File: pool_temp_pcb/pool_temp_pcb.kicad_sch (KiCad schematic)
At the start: 9 parts, among them U1 MAX7221xNG, U2 PicoW

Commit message: Update schematic
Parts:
- R1, R2, R3, R4: renamed from R?; footprint (none) -> Resistor_THT:R_Axial_DIN0411_L9.9mm_D3.6mm_P15.24mm_Horizontal
- U3, U4: renamed from U?; footprint (none) -> seven_segment:ATA8041AB
- gave numbers to parts that had none: 1

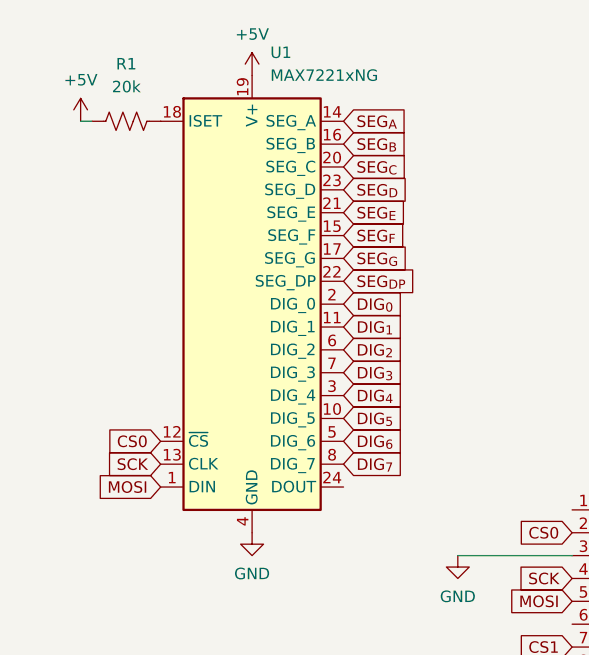
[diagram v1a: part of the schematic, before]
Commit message: Add trim pot
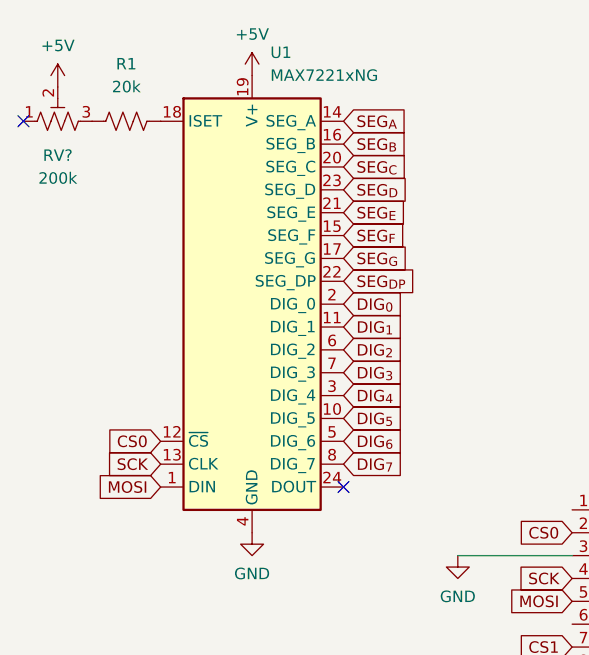
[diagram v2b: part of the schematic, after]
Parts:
- added RV?: 200k, symbol Device:R_Potentiometer_Trim_US
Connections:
- net +5V: now also RV?.2; no longer R1.1
- new net: R1.1, RV?.3
- no-connect marks 0 -> 2
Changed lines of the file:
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@@
   (junction (at 143.51 86.36) (diameter 0) (color 0 0 0 0)
   )
+  (no_connect (at 22.86 38.1))
+  (no_connect (at 58.42 78.74))
   (wire (pts (xy 125.476 81.28) (xy 119.38 81.28))
     (stroke (width 0) (type default) (color 0 0 0 0))
@@
   )
   (wire (pts (xy 143.51 96.52) (xy 147.32 96.52))
-    (stroke (width 0) (type default) (color 0 0 0 0))
-  )
-  (wire (pts (xy 29.21 38.1) (xy 30.48 38.1))
     (stroke (width 0) (type default) (color 0 0 0 0))
   )
@@
     )
     (pin "1")
+  )
+  (symbol (lib_id "Device:R_Potentiometer_Trim_US") (at 26.67 38.1 90) (unit 1)
+    (in_bom yes) (on_board yes) (fields_autoplaced)
+    (property "Reference" "RV?" (id 0) (at 26.67 41.91 90))
+    (property "Value" "200k" (id 1) (at 26.67 44.45 90))
+    (property "Footprint" "" (id 2) (at 26.67 38.1 0)
+      (effects (font (size 1.27 1.27)) hide)
+    )
+    (property "Datasheet" "~" (id 3) (at 26.67 38.1 0)
+      (effects (font (size 1.27 1.27)) hide)
+    )
+    (pin "1")
+    (pin "2")
+    (pin "3")
   )
   (symbol (lib_id "RPi_Pico:PicoW") (at 101.6 105.41 0) (unit 1)
@@
     (pin "2")
   )
-  (symbol (lib_id "power:+5V") (at 29.21 38.1 0) (unit 1)
-    (in_bom yes) (on_board yes) (fields_autoplaced)
-    (property "Reference" "#PWR01" (id 0) (at 29.21 41.91 0)
-      (effects (font (size 1.27 1.27)) hide)
-    )
-    (property "Value" "+5V" (id 1) (at 29.21 33.528 0))
-    (property "Footprint" "" (id 2) (at 29.21 38.1 0)
-      (effects (font (size 1.27 1.27)) hide)
-    )
-    (property "Datasheet" "" (id 3) (at 29.21 38.1 0)
+  (symbol (lib_id "power:+5V") (at 26.67 34.29 0) (unit 1)
+    (in_bom yes) (on_board yes) (fields_autoplaced)
+    (property "Reference" "#PWR01" (id 0) (at 26.67 38.1 0)
+      (effects (font (size 1.27 1.27)) hide)
+    )
+    (property "Value" "+5V" (id 1) (at 26.67 29.718 0))
+    (property "Footprint" "" (id 2) (at 26.67 34.29 0)
+      (effects (font (size 1.27 1.27)) hide)
+    )
+    (property "Datasheet" "" (id 3) (at 26.67 34.29 0)
       (effects (font (size 1.27 1.27)) hide)
     )
@@
       (reference "R4") (unit 1) (value "10k") (footprint "Resistor_THT:R_Axial_DIN0411_L9.9mm_D3.6mm_P15.24mm_Horizontal")
     )
+    (path "/4106378e-7235-4e9b-81fd-86d6d668a59a"
+      (reference "RV?") (unit 1) (value "200k") (footprint "")
+    )
     (path "/a163b600-67df-462c-baf5-e9cae83b8f90"

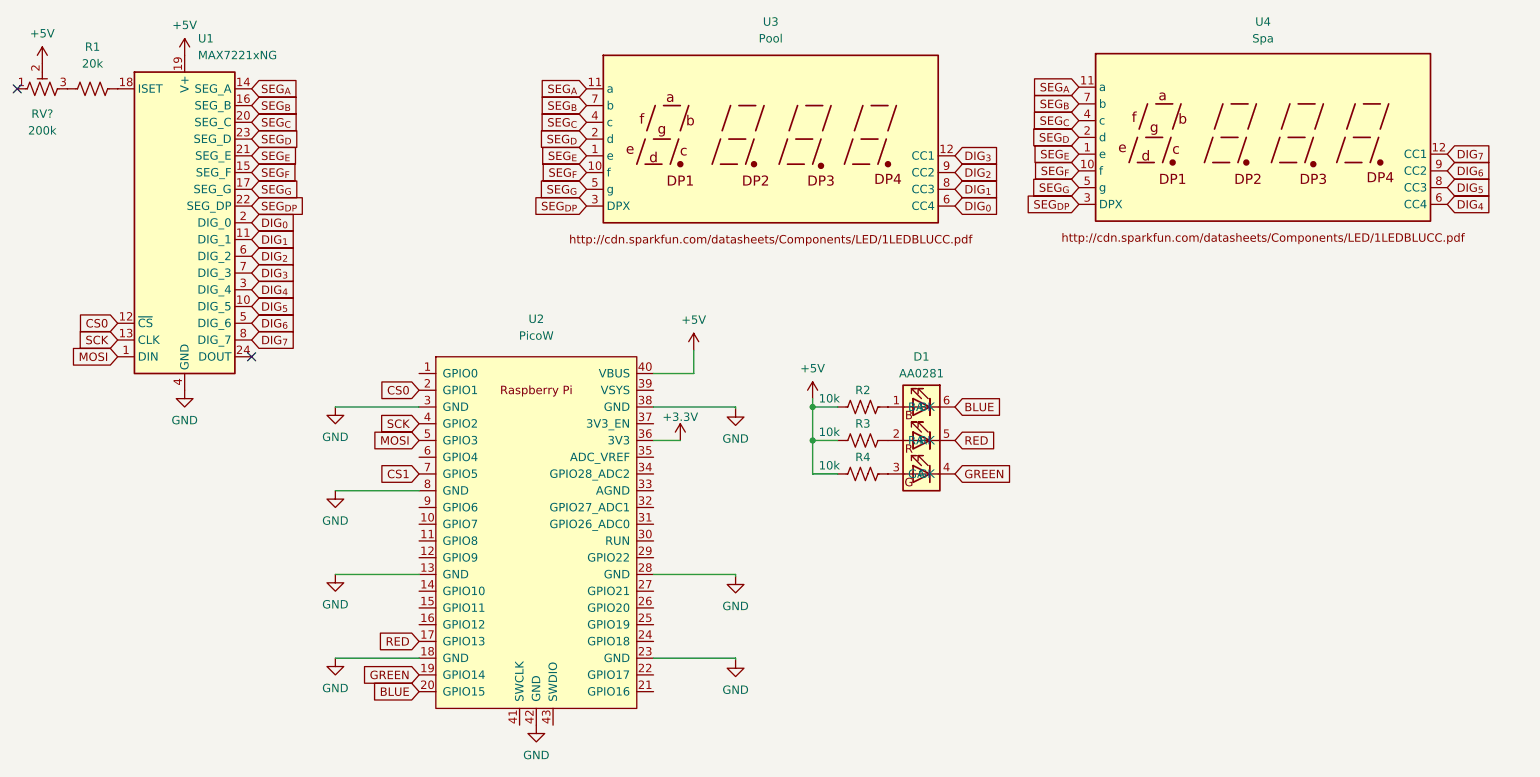
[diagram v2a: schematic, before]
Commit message: Layout version 1 of temperature pcb
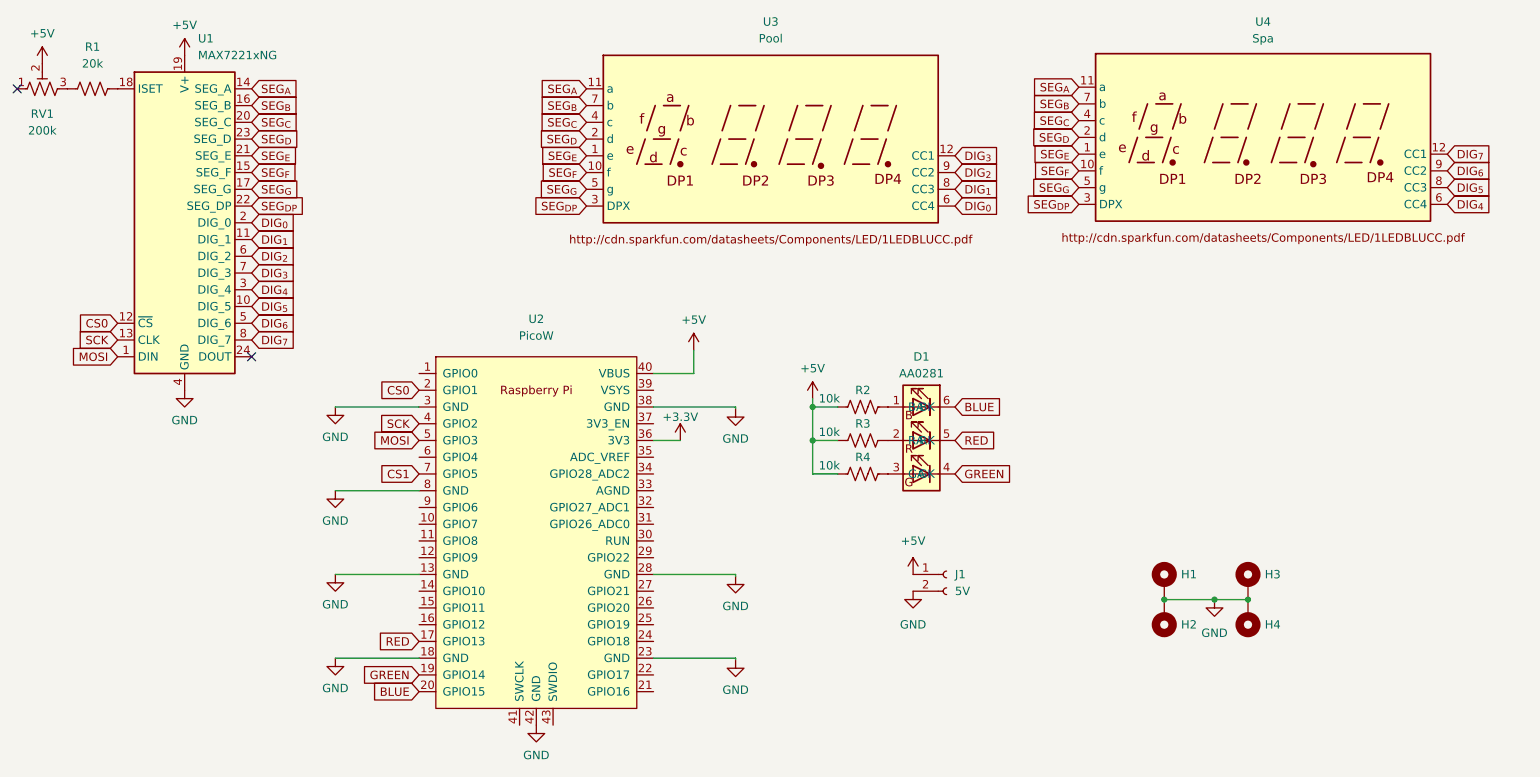
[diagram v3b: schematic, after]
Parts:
- added H1: Hole, MountingHole:MountingHole_3.2mm_M3_Pad_TopBottom, symbol Mechanical:MountingHole_Pad
- added H2, H3, H4: MountingHole_Pad, MountingHole:MountingHole_3.2mm_M3_Pad_TopBottom, symbol Mechanical:MountingHole_Pad
- added J1: 5V, Connector_PinHeader_2.54mm:PinHeader_1x02_P2.54mm_Vertical, symbol Connector:Conn_01x02_Female
- RV1: renamed from RV?; footprint (none) -> Potentiometer_THT:Potentiometer_Runtron_RM-065_Vertical
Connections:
- net +5V: now also J1.1 (Pin_1)
- net GND: now also H1.1, H2.1, H3.1, H4.1, J1.2 (Pin_2)
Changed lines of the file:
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@@
 (kicad_sch (version 20211123) (generator eeschema)
   (paper "A4")
+  (junction (at 204.47 115.57) (diameter 0) (color 0 0 0 0)
+  )
+  (junction (at 209.55 115.57) (diameter 0) (color 0 0 0 0)
+  )
   (junction (at 143.51 91.44) (diameter 0) (color 0 0 0 0)
   )
   (junction (at 143.51 86.36) (diameter 0) (color 0 0 0 0)
+  )
+  (junction (at 196.85 115.57) (diameter 0) (color 0 0 0 0)
   )
   (no_connect (at 22.86 38.1))
@@
     (stroke (width 0) (type default) (color 0 0 0 0))
   )
+  (wire (pts (xy 196.85 115.57) (xy 204.47 115.57))
+    (stroke (width 0) (type default) (color 0 0 0 0))
+  )
   (wire (pts (xy 131.826 111.76) (xy 131.826 112.014))
+    (stroke (width 0) (type default) (color 0 0 0 0))
+  )
+  (wire (pts (xy 204.47 115.57) (xy 209.55 115.57))
     (stroke (width 0) (type default) (color 0 0 0 0))
   )
@@
     )
     (property "Datasheet" "" (id 3) (at 131.826 112.014 0)
+      (effects (font (size 1.27 1.27)) hide)
+    )
+    (pin "1")
+  )
+  (symbol (lib_id "Mechanical:MountingHole_Pad") (at 196.85 113.03 0) (unit 1)
+    (in_bom yes) (on_board yes) (fields_autoplaced)
+    (property "Reference" "H1" (id 0) (at 199.39 111.7599 0)
+      (effects (font (size 1.27 1.27)) (justify left))
+    )
+    (property "Value" "Hole" (id 1) (at 199.39 113.0299 0)
+      (effects (font (size 1.27 1.27)) (justify left) hide)
+    )
+    (property "Footprint" "MountingHole:MountingHole_3.2mm_M3_Pad_TopBottom" (id 2) (at 196.85 113.03 0)
+      (effects (font (size 1.27 1.27)) hide)
+    )
+    (property "Datasheet" "~" (id 3) (at 196.85 113.03 0)
+      (effects (font (size 1.27 1.27)) hide)
+    )
+    (pin "1")
+  )
+  (symbol (lib_id "Mechanical:MountingHole_Pad") (at 209.55 118.11 180) (unit 1)
+    (in_bom yes) (on_board yes) (fields_autoplaced)
+    (property "Reference" "H4" (id 0) (at 212.09 119.3799 0)
+      (effects (font (size 1.27 1.27)) (justify right))
+    )
+    (property "Value" "MountingHole_Pad" (id 1) (at 212.09 120.6499 0)
+      (effects (font (size 1.27 1.27)) (justify right) hide)
+    )
+    (property "Footprint" "MountingHole:MountingHole_3.2mm_M3_Pad_TopBottom" (id 2) (at 209.55 118.11 0)
+      (effects (font (size 1.27 1.27)) hide)
+    )
+    (property "Datasheet" "~" (id 3) (at 209.55 118.11 0)
       (effects (font (size 1.27 1.27)) hide)
     )
@@
     (pin "1")
   )
+  (symbol (lib_id "power:GND") (at 158.75 114.3 0) (unit 1)
+    (in_bom yes) (on_board yes) (fields_autoplaced)
+    (property "Reference" "#PWR016" (id 0) (at 158.75 120.65 0)
+      (effects (font (size 1.27 1.27)) hide)
+    )
+    (property "Value" "GND" (id 1) (at 158.75 119.38 0))
+    (property "Footprint" "" (id 2) (at 158.75 114.3 0)
+      (effects (font (size 1.27 1.27)) hide)
+    )
+    (property "Datasheet" "" (id 3) (at 158.75 114.3 0)
+      (effects (font (size 1.27 1.27)) hide)
+    )
+    (pin "1")
+  )
   (symbol (lib_id "Device:R_Potentiometer_Trim_US") (at 26.67 38.1 90) (unit 1)
     (in_bom yes) (on_board yes) (fields_autoplaced)
-    (property "Reference" "RV?" (id 0) (at 26.67 41.91 90))
+    (property "Reference" "RV1" (id 0) (at 26.67 41.91 90))
     (property "Value" "200k" (id 1) (at 26.67 44.45 90))
-    (property "Footprint" "" (id 2) (at 26.67 38.1 0)
+    (property "Footprint" "Potentiometer_THT:Potentiometer_Runtron_RM-065_Vertical" (id 2) (at 26.67 38.1 0)
       (effects (font (size 1.27 1.27)) hide)
     )
@@
     (pin "1")
   )
+  (symbol (lib_id "Connector:Conn_01x02_Female") (at 163.83 111.76 0) (unit 1)
+    (in_bom yes) (on_board yes) (fields_autoplaced)
+    (property "Reference" "J1" (id 0) (at 165.1 111.7599 0)
+      (effects (font (size 1.27 1.27)) (justify left))
+    )
+    (property "Value" "5V" (id 1) (at 165.1 114.2999 0)
+      (effects (font (size 1.27 1.27)) (justify left))
+    )
+    (property "Footprint" "Connector_PinHeader_2.54mm:PinHeader_1x02_P2.54mm_Vertical" (id 2) (at 163.83 111.76 0)
+      (effects (font (size 1.27 1.27)) hide)
+    )
+    (property "Datasheet" "~" (id 3) (at 163.83 111.76 0)
+      (effects (font (size 1.27 1.27)) hide)
+    )
+    (pin "1")
+    (pin "2")
+  )
   (symbol (lib_id "power:GND") (at 101.6 134.62 0) (unit 1)
     (in_bom yes) (on_board yes) (fields_autoplaced)
@@
     (pin "1")
   )
+  (symbol (lib_id "Mechanical:MountingHole_Pad") (at 196.85 118.11 180) (unit 1)
+    (in_bom yes) (on_board yes) (fields_autoplaced)
+    (property "Reference" "H2" (id 0) (at 199.39 119.3799 0)
+      (effects (font (size 1.27 1.27)) (justify right))
+    )
+    (property "Value" "MountingHole_Pad" (id 1) (at 199.39 120.6499 0)
+      (effects (font (size 1.27 1.27)) (justify right) hide)
+    )
+    (property "Footprint" "MountingHole:MountingHole_3.2mm_M3_Pad_TopBottom" (id 2) (at 196.85 118.11 0)
+      (effects (font (size 1.27 1.27)) hide)
+    )
+    (property "Datasheet" "~" (id 3) (at 196.85 118.11 0)
+      (effects (font (size 1.27 1.27)) hide)
+    )
+    (pin "1")
+  )
   (symbol (lib_id "Device:R_US") (at 151.13 96.52 90) (unit 1)
     (in_bom yes) (on_board yes)
@@
     )
     (property "Datasheet" "" (id 3) (at 71.12 86.36 0)
+      (effects (font (size 1.27 1.27)) hide)
+    )
+    (pin "1")
+  )
+  (symbol (lib_id "power:GND") (at 204.47 115.57 0) (unit 1)
+    (in_bom yes) (on_board yes) (fields_autoplaced)
+    (property "Reference" "#PWR017" (id 0) (at 204.47 121.92 0)
+      (effects (font (size 1.27 1.27)) hide)
+    )
+    (property "Value" "GND" (id 1) (at 204.47 120.65 0))
+    (property "Footprint" "" (id 2) (at 204.47 115.57 0)
+      (effects (font (size 1.27 1.27)) hide)
+    )
+    (property "Datasheet" "" (id 3) (at 204.47 115.57 0)
       (effects (font (size 1.27 1.27)) hide)
     )
@@
     (pin "2")
   )
+  (symbol (lib_id "power:+5V") (at 158.75 111.76 0) (unit 1)
+    (in_bom yes) (on_board yes) (fields_autoplaced)
+    (property "Reference" "#PWR015" (id 0) (at 158.75 115.57 0)
+      (effects (font (size 1.27 1.27)) hide)
+    )
+    (property "Value" "+5V" (id 1) (at 158.75 106.68 0))
+    (property "Footprint" "" (id 2) (at 158.75 111.76 0)
+      (effects (font (size 1.27 1.27)) hide)
+    )
+    (property "Datasheet" "" (id 3) (at 158.75 111.76 0)
+      (effects (font (size 1.27 1.27)) hide)
+    )
+    (pin "1")
+  )
   (symbol (lib_id "seven_segment:ATA8041AB") (at 137.16 45.72 0) (unit 1)
     (in_bom yes) (on_board yes) (fields_autoplaced)
@@
     (pin "9")
   )
+  (symbol (lib_id "Mechanical:MountingHole_Pad") (at 209.55 113.03 0) (unit 1)
+    (in_bom yes) (on_board yes) (fields_autoplaced)
+    (property "Reference" "H3" (id 0) (at 212.09 111.7599 0)
+      (effects (font (size 1.27 1.27)) (justify left))
+    )
+    (property "Value" "MountingHole_Pad" (id 1) (at 212.09 113.0299 0)
+      (effects (font (size 1.27 1.27)) (justify left) hide)
+    )
+    (property "Footprint" "MountingHole:MountingHole_3.2mm_M3_Pad_TopBottom" (id 2) (at 209.55 113.03 0)
+      (effects (font (size 1.27 1.27)) hide)
+    )
+    (property "Datasheet" "~" (id 3) (at 209.55 113.03 0)
+      (effects (font (size 1.27 1.27)) hide)
+    )
+    (pin "1")
+  )
   (symbol (lib_id "power:GND") (at 71.12 111.76 0) (unit 1)
     (in_bom yes) (on_board yes) (fields_autoplaced)
@@
       (reference "#PWR014") (unit 1) (value "+5V") (footprint "")
     )
+    (path "/c01cdd70-f30b-4244-ae49-602d6e50a405"
+      (reference "#PWR015") (unit 1) (value "+5V") (footprint "")
+    )
+    (path "/39e81ee3-f1b1-47b7-a57f-81462ea3acdf"
+      (reference "#PWR016") (unit 1) (value "GND") (footprint "")
+    )
+    (path "/9224d574-e5c3-4a9b-9b90-c97541b1cfe2"
+      (reference "#PWR017") (unit 1) (value "GND") (footprint "")
+    )
     (path "/31a6f4dd-9e1d-4a25-898e-8aabb01b24dc"
       (reference "D1") (unit 1) (value "AA0281") (footprint "LED_SMD:LED_RGB_5050-6")
     )
+    (path "/0c56ea47-6297-4be9-82c4-67319187963f"
+      (reference "H1") (unit 1) (value "Hole") (footprint "MountingHole:MountingHole_3.2mm_M3_Pad_TopBottom")
+    )
+    (path "/70be384c-ffe2-42d0-b4b5-b801068b56a6"
+      (reference "H2") (unit 1) (value "MountingHole_Pad") (footprint "MountingHole:MountingHole_3.2mm_M3_Pad_TopBottom")
+    )
+    (path "/c377a767-14ac-4f60-978d-353e0b2ec5e9"
+      (reference "H3") (unit 1) (value "MountingHole_Pad") (footprint "MountingHole:MountingHole_3.2mm_M3_Pad_TopBottom")
+    )
+    (path "/21286bce-f682-4442-9173-0d667d8438e7"
+      (reference "H4") (unit 1) (value "MountingHole_Pad") (footprint "MountingHole:MountingHole_3.2mm_M3_Pad_TopBottom")
+    )
+    (path "/54be0a1f-9dc7-4bc8-b267-224774b5b318"
+      (reference "J1") (unit 1) (value "5V") (footprint "Connector_PinHeader_2.54mm:PinHeader_1x02_P2.54mm_Vertical")
+    )
     (path "/35184f82-3958-45d2-8361-36930c82ffcb"
       (reference "R1") (unit 1) (value "20k") (footprint "Resistor_THT:R_Axial_DIN0411_L9.9mm_D3.6mm_P15.24mm_Horizontal")
@@
     )
     (path "/4106378e-7235-4e9b-81fd-86d6d668a59a"
-      (reference "RV?") (unit 1) (value "200k") (footprint "")
+      (reference "RV1") (unit 1) (value "200k") (footprint "Potentiometer_THT:Potentiometer_Runtron_RM-065_Vertical")
     )
     (path "/a163b600-67df-462c-baf5-e9cae83b8f90"
